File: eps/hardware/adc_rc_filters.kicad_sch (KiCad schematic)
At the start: 20 parts

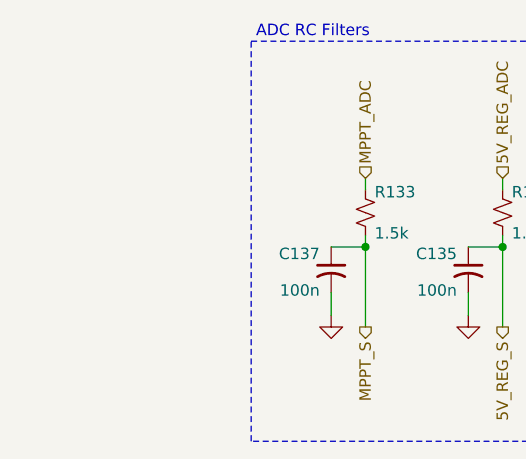
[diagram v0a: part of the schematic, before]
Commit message: fix ERC issue in LTC3130-1
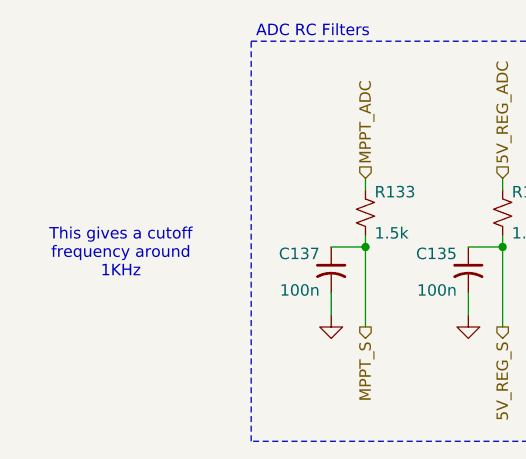
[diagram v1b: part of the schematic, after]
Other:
- note added: "This gives a cutoff frequency around 1KHz"
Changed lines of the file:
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@@
+		)
+	)
+	(text "This gives a cutoff\nfrequency around\n1KHz"
+		(exclude_from_sim no)
+		(at 52.832 94.742 0)
+		(effects
+			(font
+				(size 1.27 1.27)
+			)
 		)
 	)

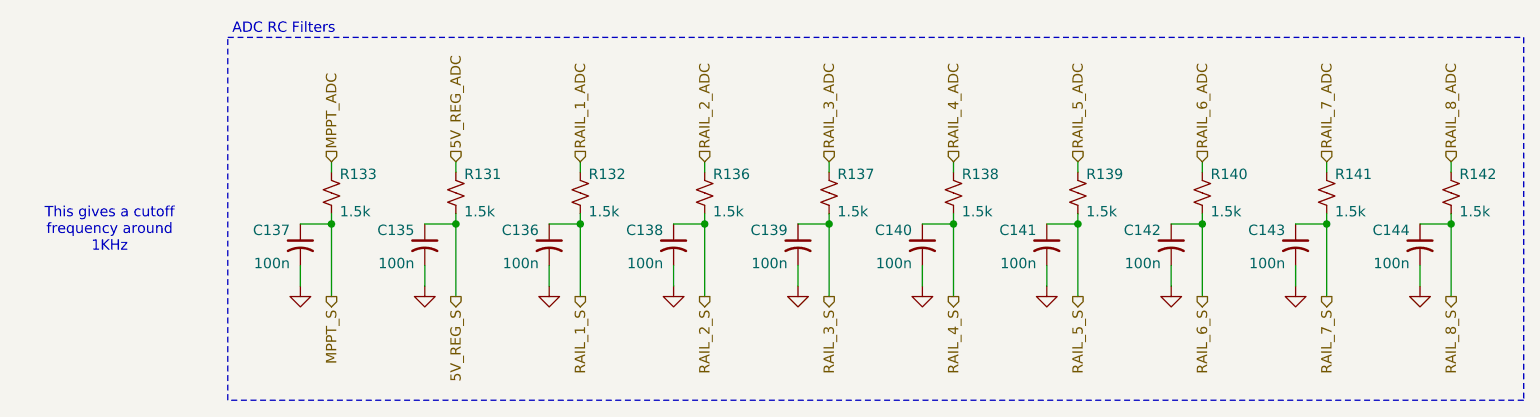
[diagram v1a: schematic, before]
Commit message: fix all ERC errors
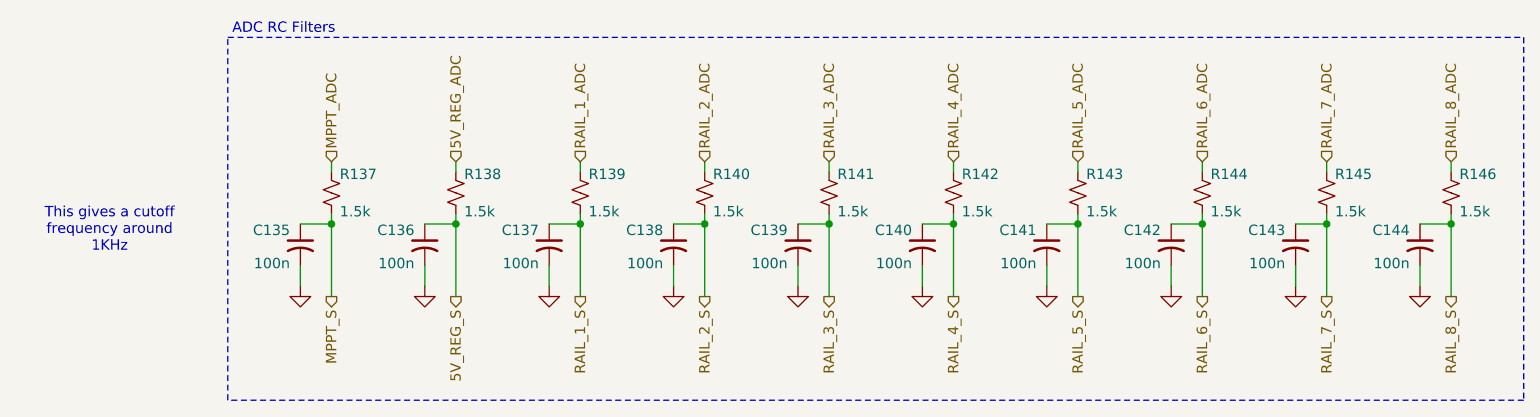
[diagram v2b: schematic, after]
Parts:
- renumbered C137 to C135, C135 to C136, C136 to C137, R133 to R137, R131 to R138, R132 to R139, R136 to R140, R137 to R141, R138 to R142, R139 to R143, R140 to R144, R141 to R145, R142 to R146

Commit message: start footprint assignment
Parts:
- C135, C136, C137, C138, C139, C140, C141, C142, C143, C144: footprint (none) -> Capacitor_SMD:C_0603_1608Metric
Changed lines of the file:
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@@
 			)
 		)
-		(property "Footprint" ""
+		(property "Footprint" "Capacitor_SMD:C_0603_1608Metric"
 			(at 182.88 96.52 0)
 			(effects
@@
 			)
 		)
-		(property "Footprint" ""
+		(property "Footprint" "Capacitor_SMD:C_0603_1608Metric"
 			(at 121.92 96.52 0)
 			(effects
@@
 			)
 		)
-		(property "Footprint" ""
+		(property "Footprint" "Capacitor_SMD:C_0603_1608Metric"
 			(at 137.16 96.52 0)
 			(effects
@@
 			)
 		)
-		(property "Footprint" ""
+		(property "Footprint" "Capacitor_SMD:C_0603_1608Metric"
 			(at 152.4 96.52 0)
 			(effects
@@
 			)
 		)
-		(property "Footprint" ""
+		(property "Footprint" "Capacitor_SMD:C_0603_1608Metric"
 			(at 106.68 96.52 0)
 			(effects
@@
 			)
 		)
-		(property "Footprint" ""
+		(property "Footprint" "Capacitor_SMD:C_0603_1608Metric"
 			(at 198.12 96.52 0)
 			(effects
@@
 			)
 		)
-		(property "Footprint" ""
+		(property "Footprint" "Capacitor_SMD:C_0603_1608Metric"
 			(at 76.2 96.52 0)
 			(effects
@@
 			)
 		)
-		(property "Footprint" ""
+		(property "Footprint" "Capacitor_SMD:C_0603_1608Metric"
 			(at 167.64 96.52 0)
 			(effects
@@
 			)
 		)
-		(property "Footprint" ""
+		(property "Footprint" "Capacitor_SMD:C_0603_1608Metric"
 			(at 213.36 96.52 0)
 			(effects
@@
 			)
 		)
-		(property "Footprint" ""
+		(property "Footprint" "Capacitor_SMD:C_0603_1608Metric"
 			(at 91.44 96.52 0)
 			(effects

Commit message: finish footprint assignment and board setup
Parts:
- R137, R138, R139, R140, R141, R142, R143, R144, R145, R146: footprint (none) -> Resistor_SMD:R_0603_1608Metric
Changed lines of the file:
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@@
 			)
 		)
-		(property "Footprint" ""
+		(property "Footprint" "Resistor_SMD:R_0603_1608Metric"
 			(at 80.01 90.17 0)
 			(effects
@@
 			)
 		)
-		(property "Footprint" ""
+		(property "Footprint" "Resistor_SMD:R_0603_1608Metric"
 			(at 125.73 90.17 0)
 			(effects
@@
 			)
 		)
-		(property "Footprint" ""
+		(property "Footprint" "Resistor_SMD:R_0603_1608Metric"
 			(at 110.49 90.17 0)
 			(effects
@@
 			)
 		)
-		(property "Footprint" ""
+		(property "Footprint" "Resistor_SMD:R_0603_1608Metric"
 			(at 140.97 90.17 0)
 			(effects
@@
 			)
 		)
-		(property "Footprint" ""
+		(property "Footprint" "Resistor_SMD:R_0603_1608Metric"
 			(at 201.93 90.17 0)
 			(effects
@@
 			)
 		)
-		(property "Footprint" ""
+		(property "Footprint" "Resistor_SMD:R_0603_1608Metric"
 			(at 95.25 90.17 0)
 			(effects
@@
 			)
 		)
-		(property "Footprint" ""
+		(property "Footprint" "Resistor_SMD:R_0603_1608Metric"
 			(at 171.45 90.17 0)
 			(effects
@@
 			)
 		)
-		(property "Footprint" ""
+		(property "Footprint" "Resistor_SMD:R_0603_1608Metric"
 			(at 217.17 90.17 0)
 			(effects
@@
 			)
 		)
-		(property "Footprint" ""
+		(property "Footprint" "Resistor_SMD:R_0603_1608Metric"
 			(at 186.69 90.17 0)
 			(effects
@@
 			)
 		)
-		(property "Footprint" ""
+		(property "Footprint" "Resistor_SMD:R_0603_1608Metric"
 			(at 156.21 90.17 0)
 			(effects

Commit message: schematic fixes
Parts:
- C135, C136, C137, C138, C139, C140, C141, C142, C143, C144: footprint Capacitor_SMD:C_0603_1608Metric -> Capacitor_SMD:C_0402_1005Metric
- R137, R138, R139, R140, R141, R142, R143, R144, R145, R146: footprint Resistor_SMD:R_0603_1608Metric -> Resistor_SMD:R_0402_1005Metric
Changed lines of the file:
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@@
 			)
 		)
-		(property "Footprint" "Capacitor_SMD:C_0603_1608Metric"
+		(property "Footprint" "Capacitor_SMD:C_0402_1005Metric"
 			(at 182.88 96.52 0)
 			(effects
@@
 			)
 		)
-		(property "Footprint" "Capacitor_SMD:C_0603_1608Metric"
+		(property "Footprint" "Capacitor_SMD:C_0402_1005Metric"
 			(at 121.92 96.52 0)
 			(effects
@@
 			)
 		)
-		(property "Footprint" "Capacitor_SMD:C_0603_1608Metric"
+		(property "Footprint" "Capacitor_SMD:C_0402_1005Metric"
 			(at 137.16 96.52 0)
 			(effects
@@
 			)
 		)
-		(property "Footprint" "Resistor_SMD:R_0603_1608Metric"
+		(property "Footprint" "Resistor_SMD:R_0402_1005Metric"
 			(at 80.01 90.17 0)
 			(effects
@@
 			)
 		)
-		(property "Footprint" "Capacitor_SMD:C_0603_1608Metric"
+		(property "Footprint" "Capacitor_SMD:C_0402_1005Metric"
 			(at 152.4 96.52 0)
 			(effects
@@
 			)
 		)
-		(property "Footprint" "Resistor_SMD:R_0603_1608Metric"
+		(property "Footprint" "Resistor_SMD:R_0402_1005Metric"
 			(at 125.73 90.17 0)
 			(effects
@@
 			)
 		)
-		(property "Footprint" "Capacitor_SMD:C_0603_1608Metric"
+		(property "Footprint" "Capacitor_SMD:C_0402_1005Metric"
 			(at 106.68 96.52 0)
 			(effects
@@
 			)
 		)
-		(property "Footprint" "Capacitor_SMD:C_0603_1608Metric"
+		(property "Footprint" "Capacitor_SMD:C_0402_1005Metric"
 			(at 198.12 96.52 0)
 			(effects
@@
 			)
 		)
-		(property "Footprint" "Resistor_SMD:R_0603_1608Metric"
+		(property "Footprint" "Resistor_SMD:R_0402_1005Metric"
 			(at 110.49 90.17 0)
 			(effects
@@
 			)
 		)
-		(property "Footprint" "Capacitor_SMD:C_0603_1608Metric"
+		(property "Footprint" "Capacitor_SMD:C_0402_1005Metric"
 			(at 76.2 96.52 0)
 			(effects
@@
 			)
 		)
-		(property "Footprint" "Resistor_SMD:R_0603_1608Metric"
+		(property "Footprint" "Resistor_SMD:R_0402_1005Metric"
 			(at 140.97 90.17 0)
 			(effects
@@
 			)
 		)
-		(property "Footprint" "Resistor_SMD:R_0603_1608Metric"
+		(property "Footprint" "Resistor_SMD:R_0402_1005Metric"
 			(at 201.93 90.17 0)
 			(effects
@@
 			)
 		)
-		(property "Footprint" "Resistor_SMD:R_0603_1608Metric"
+		(property "Footprint" "Resistor_SMD:R_0402_1005Metric"
 			(at 95.25 90.17 0)
 			(effects
@@
 			)
 		)
-		(property "Footprint" "Capacitor_SMD:C_0603_1608Metric"
+		(property "Footprint" "Capacitor_SMD:C_0402_1005Metric"
 			(at 167.64 96.52 0)
 			(effects
@@
 			)
 		)
-		(property "Footprint" "Resistor_SMD:R_0603_1608Metric"
+		(property "Footprint" "Resistor_SMD:R_0402_1005Metric"
 			(at 171.45 90.17 0)
 			(effects
@@
 			)
 		)
-		(property "Footprint" "Resistor_SMD:R_0603_1608Metric"
+		(property "Footprint" "Resistor_SMD:R_0402_1005Metric"
 			(at 217.17 90.17 0)
 			(effects
@@
 			)
 		)
-		(property "Footprint" "Capacitor_SMD:C_0603_1608Metric"
+		(property "Footprint" "Capacitor_SMD:C_0402_1005Metric"
 			(at 213.36 96.52 0)
 			(effects
@@
 			)
 		)
-		(property "Footprint" "Capacitor_SMD:C_0603_1608Metric"
+		(property "Footprint" "Capacitor_SMD:C_0402_1005Metric"
 			(at 91.44 96.52 0)
 			(effects
@@
 			)
 		)
-		(property "Footprint" "Resistor_SMD:R_0603_1608Metric"
+		(property "Footprint" "Resistor_SMD:R_0402_1005Metric"
 			(at 186.69 90.17 0)
 			(effects
@@
 			)
 		)
-		(property "Footprint" "Resistor_SMD:R_0603_1608Metric"
+		(property "Footprint" "Resistor_SMD:R_0402_1005Metric"
 			(at 156.21 90.17 0)
 			(effects

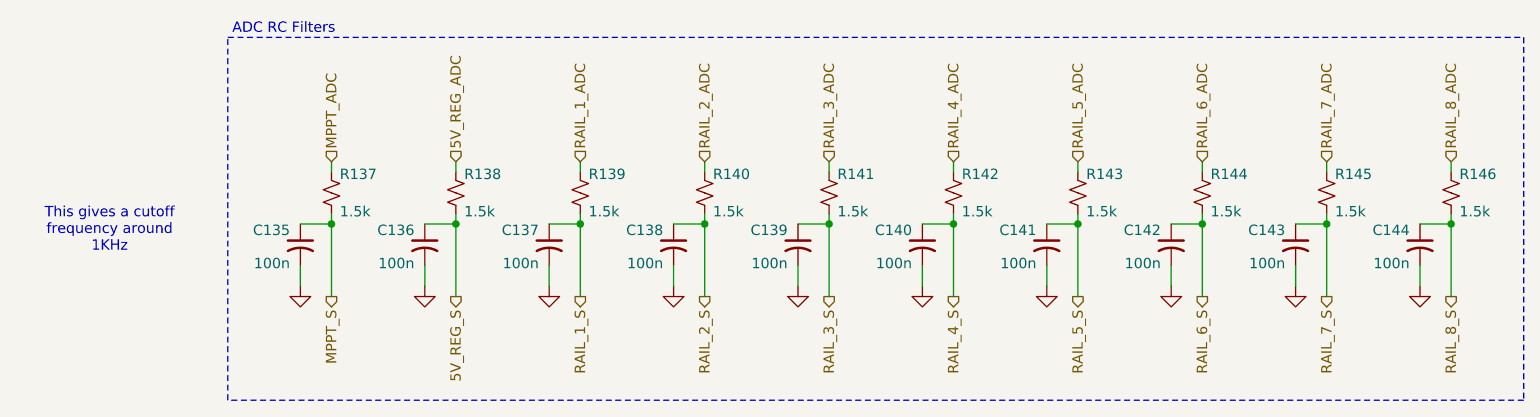
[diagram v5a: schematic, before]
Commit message: add BOM and fix tons of hardware bugs
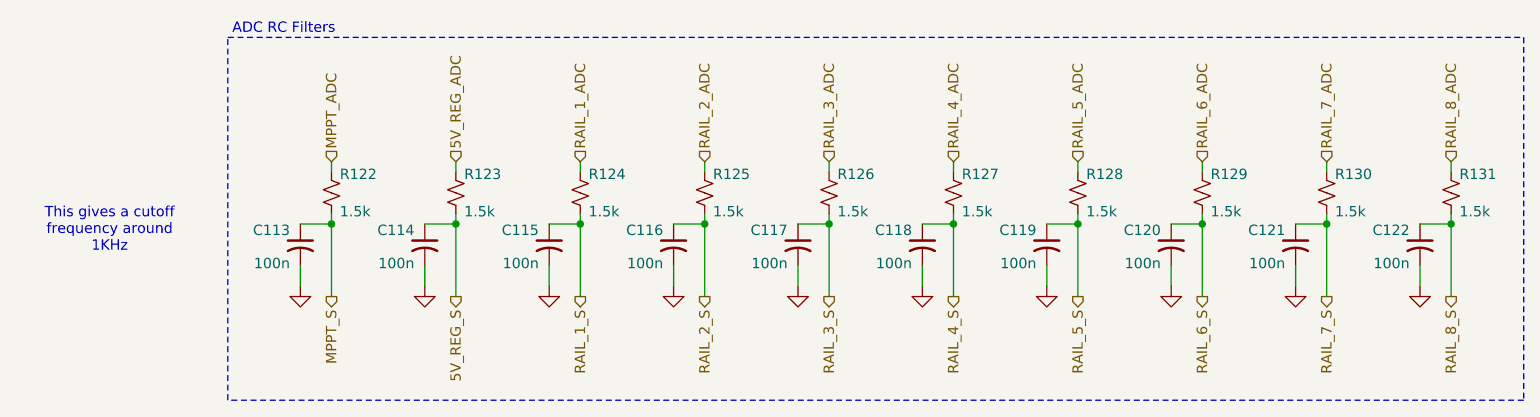
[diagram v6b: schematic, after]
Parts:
- C113: renamed from C135; LCSC PN (none) -> C1525
- C114: renamed from C136; LCSC PN (none) -> C1525
- C115: renamed from C137; LCSC PN (none) -> C1525
- C116: renamed from C138; LCSC PN (none) -> C1525
- C117: renamed from C139; LCSC PN (none) -> C1525
- C118: renamed from C140; LCSC PN (none) -> C1525
- C119: renamed from C141; LCSC PN (none) -> C1525
- C120: renamed from C142; LCSC PN (none) -> C1525
- C121: renamed from C143; LCSC PN (none) -> C1525
- C122: renamed from C144; LCSC PN (none) -> C1525
- R122: renamed from R137; LCSC PN (none) -> C25867
- R123: renamed from R138; LCSC PN (none) -> C25867
- R124: renamed from R139; LCSC PN (none) -> C25867
- R125: renamed from R140; LCSC PN (none) -> C25867
- R126: renamed from R141; LCSC PN (none) -> C25867
- R127: renamed from R142; LCSC PN (none) -> C25867
- R128: renamed from R143; LCSC PN (none) -> C25867
- R129: renamed from R144; LCSC PN (none) -> C25867
- R130: renamed from R145; LCSC PN (none) -> C25867
- R131: renamed from R146; LCSC PN (none) -> C25867
